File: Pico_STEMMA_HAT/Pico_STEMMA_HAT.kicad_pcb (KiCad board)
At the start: 2 copper layers, 58 x 67 mm, 57 parts, among them J1 Conn_01x20_Socket, J2 Conn_01x20_Socket, J3 SDCARD_MODULE

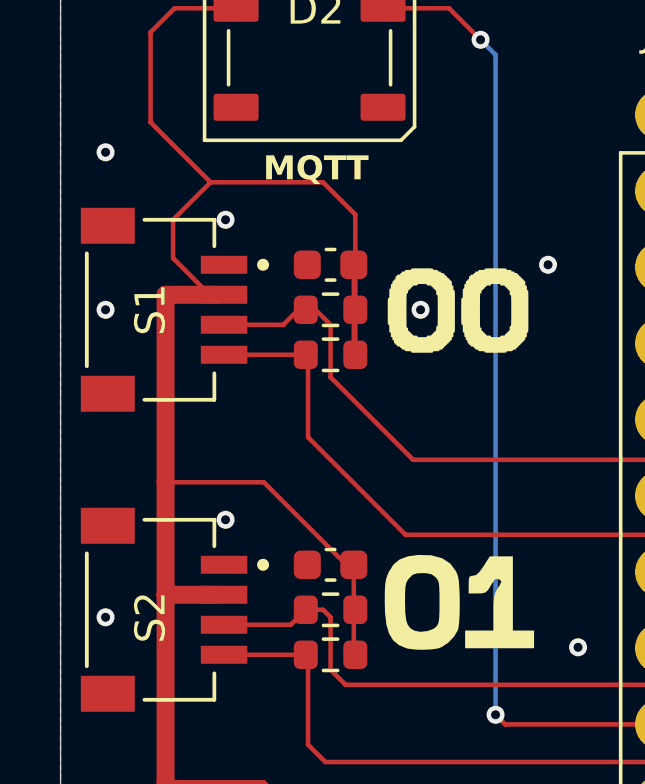
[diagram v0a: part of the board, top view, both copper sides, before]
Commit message: Adjust traces
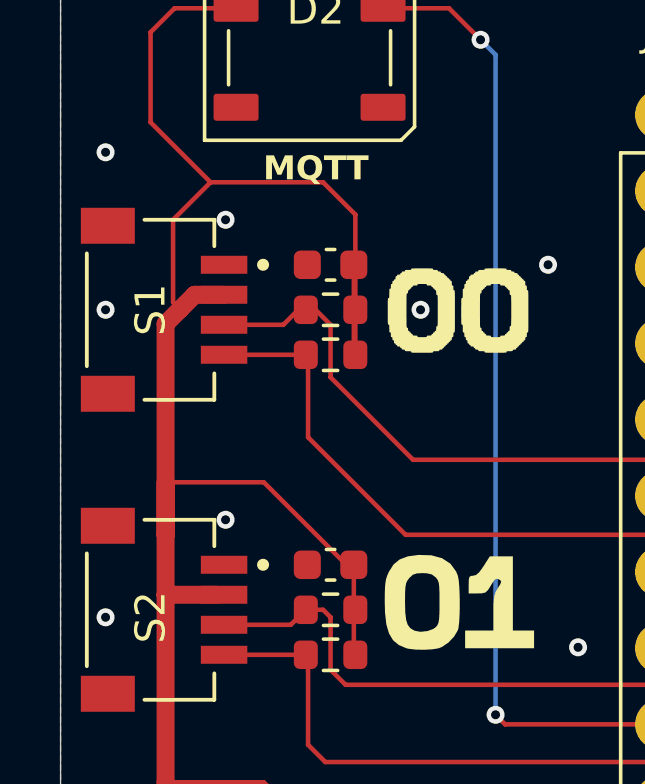
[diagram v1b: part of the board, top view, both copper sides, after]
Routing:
- net +3V3: track 376.0 -> 377.0 mm
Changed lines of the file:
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@@
 		)
 		(property "Value" "0.1 uF"
-			(at 0 1.43 90)
+			(at 1 2 90)
 			(layer "F.Fab")
 			(effects
@@
 		)
 		(property "Value" "4.7k"
-			(at 0 1.43 90)
+			(at -3.25 0 90)
 			(layer "F.Fab")
 			(effects
@@
 		)
 		(property "Value" "4.7k"
-			(at 0 1.43 90)
+			(at -3.25 0 90)
 			(layer "F.Fab")
 			(effects
@@
 	)
 	(segment
+		(start 124.9851 84.9851)
+		(end 125.4702 84.5)
+		(width 0.6)
+		(layer "F.Cu")
+		(net 2)
+	)
+	(segment
+		(start 124.5 94.5)
+		(end 124.5 92.5)
+		(width 0.6)
+		(layer "F.Cu")
+		(net 2)
+	)
+	(segment
 		(start 173 120)
 		(end 169.675 116.675)
@@
 	)
 	(segment
-		(start 126.2 84.5)
-		(end 124.5 84.5)
-		(width 0.6)
-		(layer "F.Cu")
-		(net 2)
-	)
-	(segment
 		(start 130.775 83.5)
 		(end 130.775 86.45)
@@
 	)
 	(segment
+		(start 125.4702 84.5)
+		(end 126.45 84.5)
+		(width 0.6)
+		(layer "F.Cu")
+		(net 2)
+	)
+	(segment
 		(start 148.5 137.5)
 		(end 143 137.5)
@@
 	)
 	(segment
-		(start 124.5 90.75)
-		(end 124.5 84.5)
-		(width 0.6)
-		(layer "F.Cu")
-		(net 2)
-	)
-	(segment
 		(start 169.725 116.5)
 		(end 166.075 116.5)
@@
 	)
 	(segment
+		(start 124.75 84.75)
+		(end 124.9851 84.9851)
+		(width 0.1524)
+		(layer "F.Cu")
+		(net 2)
+	)
+	(segment
 		(start 130.525 93.5)
 		(end 127.775 90.75)
@@
 	)
 	(segment
+		(start 124.5 92.5)
+		(end 124.5 85.4702)
+		(width 0.6)
+		(layer "F.Cu")
+		(net 2)
+	)
+	(segment
 		(start 130.775 103.5)
 		(end 130.775 106.45)
@@
 	)
 	(segment
-		(start 125.971 84.5)
-		(end 124.75 83.279)
-		(width 0.1524)
-		(layer "F.Cu")
-		(net 2)
-	)
-	(segment
 		(start 126 80.75)
 		(end 129.75 80.75)
@@
 	)
 	(segment
-		(start 124.5 94.5)
-		(end 124.5 90.75)
-		(width 0.6)
-		(layer "F.Cu")
-		(net 2)
-	)
-	(segment
-		(start 126.45 84.5)
-		(end 125.971 84.5)
-		(width 0.1524)
-		(layer "F.Cu")
-		(net 2)
-	)
-	(segment
 		(start 174.05 105.5)
 		(end 175.75 105.5)
@@
 	)
 	(segment
-		(start 124.75 82)
-		(end 126 80.75)
-		(width 0.1524)
-		(layer "F.Cu")
-		(net 2)
-	)
-	(segment
 		(start 169.725 83.55)
 		(end 169.725 86.725)
@@
 	)
 	(segment
+		(start 124.5 92.5)
+		(end 124.5 90.75)
+		(width 0.6)
+		(layer "F.Cu")
+		(net 2)
+	)
+	(segment
 		(start 130.525 103.5)
 		(end 127.775 100.75)
@@
 	)
 	(segment
+		(start 124.75 82)
+		(end 124.75 84.75)
+		(width 0.1524)
+		(layer "F.Cu")
+		(net 2)
+	)
+	(segment
 		(start 169.725 86.725)
 		(end 172.5 89.5)
@@
 	)
 	(segment
+		(start 124.5 85.4702)
+		(end 124.9851 84.9851)
+		(width 0.6)
+		(layer "F.Cu")
+		(net 2)
+	)
+	(segment
 		(start 175.75 109.75)
 		(end 173 109.75)
@@
 	)
 	(segment
-		(start 124.75 83.279)
-		(end 124.75 82)
-		(width 0.1524)
-		(layer "F.Cu")
-		(net 2)
-	)
-	(segment
 		(start 157.725 133.5)
 		(end 157.725 136.725)
@@
 		(layer "F.Cu")
 		(net 2)
+	)
+	(segment
+		(start 126 80.75)
+		(end 124.75 82)
+		(width 0.1524)
+		(layer "F.Cu")
+		(net 2)

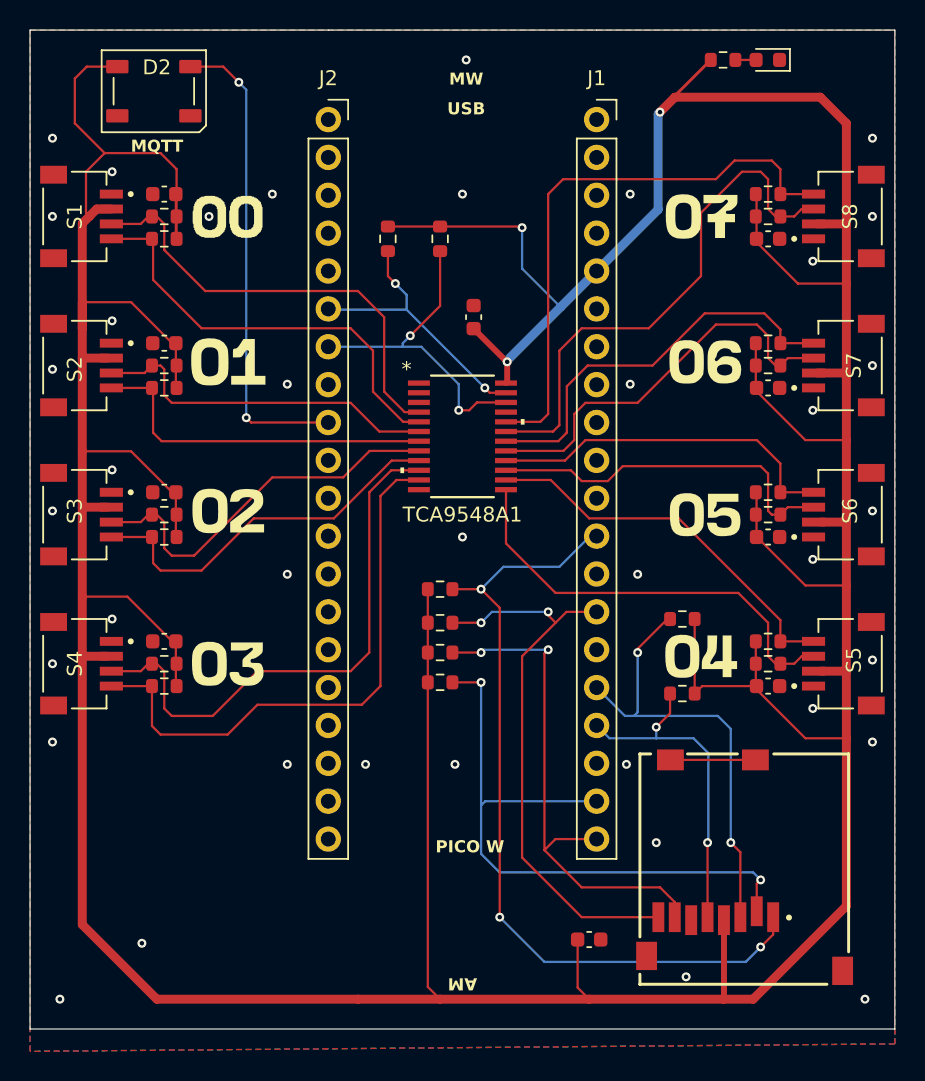
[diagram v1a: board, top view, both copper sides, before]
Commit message: Add the ability to change multiplexer address
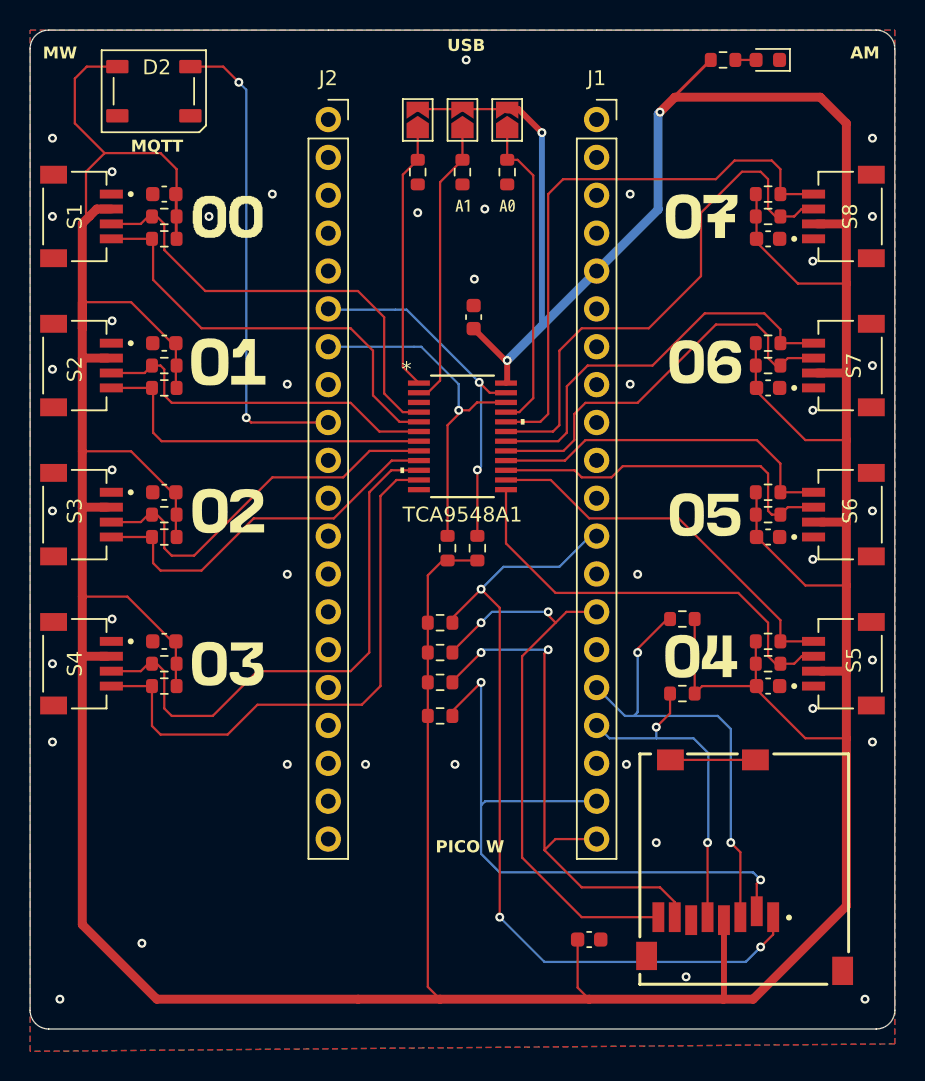
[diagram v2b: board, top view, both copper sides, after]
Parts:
- added JP1: SolderJumper_2_Open, Jumper:SolderJumper-2_P1.3mm_Open_TrianglePad1.0x1.5mm, F.Cu at (153.0, 78.5)
- added JP2: SolderJumper_2_Open, Jumper:SolderJumper-2_P1.3mm_Open_TrianglePad1.0x1.5mm, F.Cu at (150.0, 78.5)
- added JP3: SolderJumper_2_Open, Jumper:SolderJumper-2_P1.3mm_Open_TrianglePad1.0x1.5mm, F.Cu at (147.0, 78.5)
- added R26: 10k, Resistor_SMD:R_0603_1608Metric, F.Cu at (153.0, 82.0)
- added R27: 10k, Resistor_SMD:R_0603_1608Metric, F.Cu at (150.0, 82.0)
- added R28: 10k, Resistor_SMD:R_0603_1608Metric, F.Cu at (147.0, 82.0)
- added kibuzzard-67A6AC81: G***, kibuzzard-67A6AC81, F.Cu at (153.0, 84.3)
- added kibuzzard-67A6AC93: G***, kibuzzard-67A6AC93, F.Cu at (150.0, 84.3)
- moved R25 21.6 mm to (151.0, 107.2), turned to 90 degrees
- moved R24 20.8 mm to (149.0, 107.2), turned to 90 degrees
- moved R20 2.25 mm to (148.5, 118.5)
- moved R21 2.25 mm to (148.5, 112.2)
- moved R22 2.00 mm to (148.5, 114.2)
- moved R23 2.00 mm to (148.5, 116.2)
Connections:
- TCA9548A1 pad 1: unconnected-(TCA9548A1-A0-Pad1) -> /A2
- TCA9548A1 pad 2: unconnected-(TCA9548A1-A1-Pad2) -> /A1
- TCA9548A1 pad 21: unconnected-(TCA9548A1-A2-Pad21) -> /A0
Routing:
- net /A0: track 0.00 -> 21.3 mm
- net /A1: track 0.00 -> 19.1 mm
- net /A2: track 0.00 -> 17.8 mm
- net +3V3: track 377.0 -> 388.6 mm
- net /PICO_SDA: track 18.7 -> 24.7 mm
- net /PICO_SCL: track 22.4 -> 23.7 mm, vias 2 -> 1
- net /GPIO22/DAT2: track 55.2 -> 56.4 mm
- net /GPIO17/CS: track 43.0 -> 44.1 mm
- net /GPIO21/DAT1: track 38.2 -> 39.1 mm
- net /GPIO16/DATA_OUT: track 35.0 -> 35.9 mm
- net GND: vias 39 -> 40
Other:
- outline, holes or cut-outs redrawn

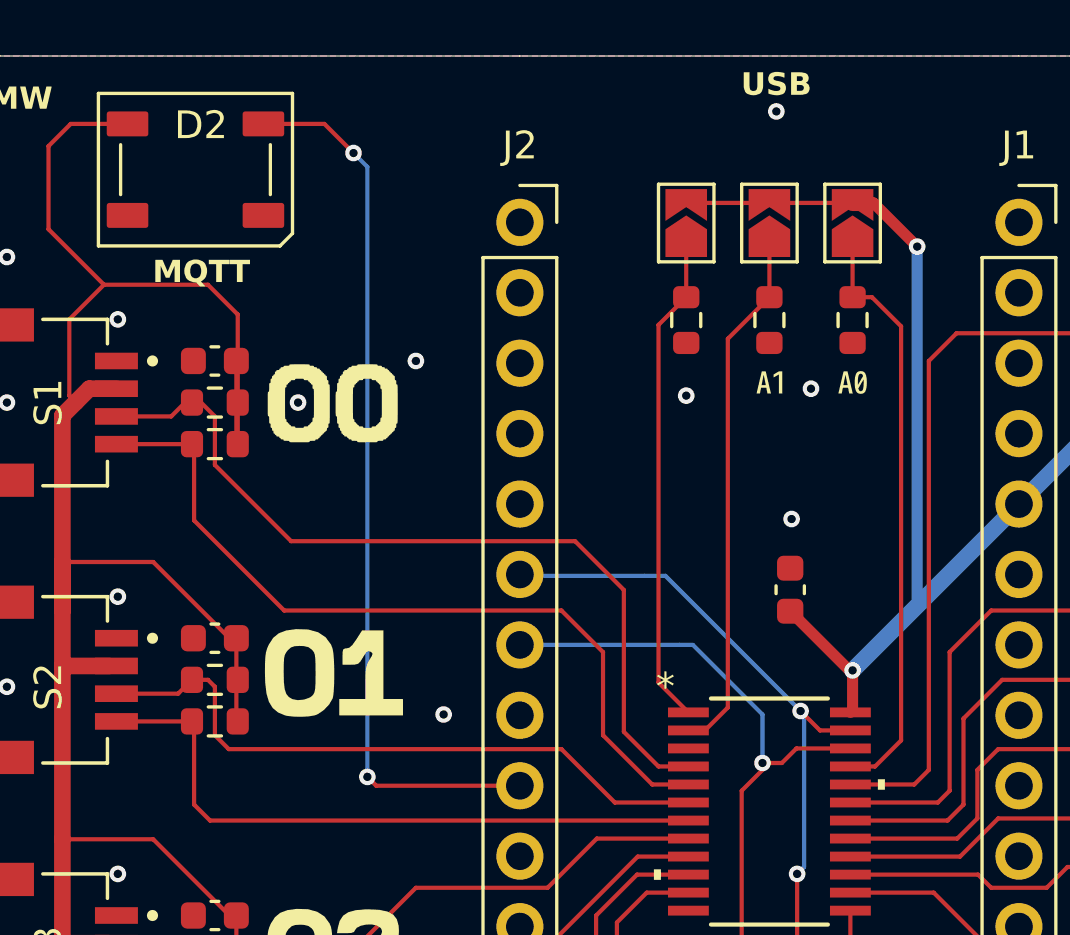
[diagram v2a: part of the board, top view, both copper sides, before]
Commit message: Adjust traces
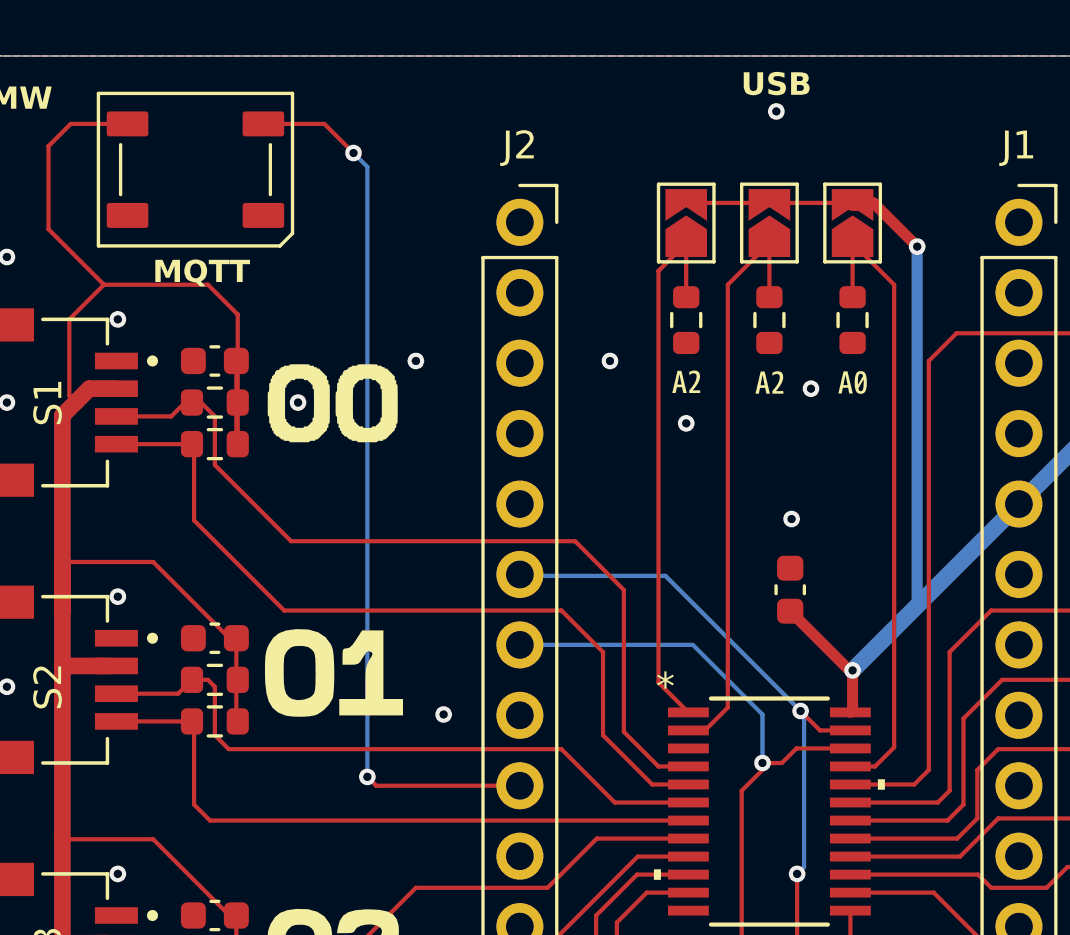
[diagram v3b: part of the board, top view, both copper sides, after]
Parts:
- removed kibuzzard-67A6AC93: G***, kibuzzard-67A6AC93
- added kibuzzard-67A6B8FA: G***, kibuzzard-67A6B8FA, F.Cu at (150.0, 84.3)
- added kibuzzard-67A6B903: G***, kibuzzard-67A6B903, F.Cu at (147.0, 84.2)
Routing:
- net /A2: track 17.8 -> 19.7 mm
- net /A1: track 19.1 -> 21.1 mm
- net /A0: track 21.3 -> 22.6 mm
- net GND: vias 40 -> 41

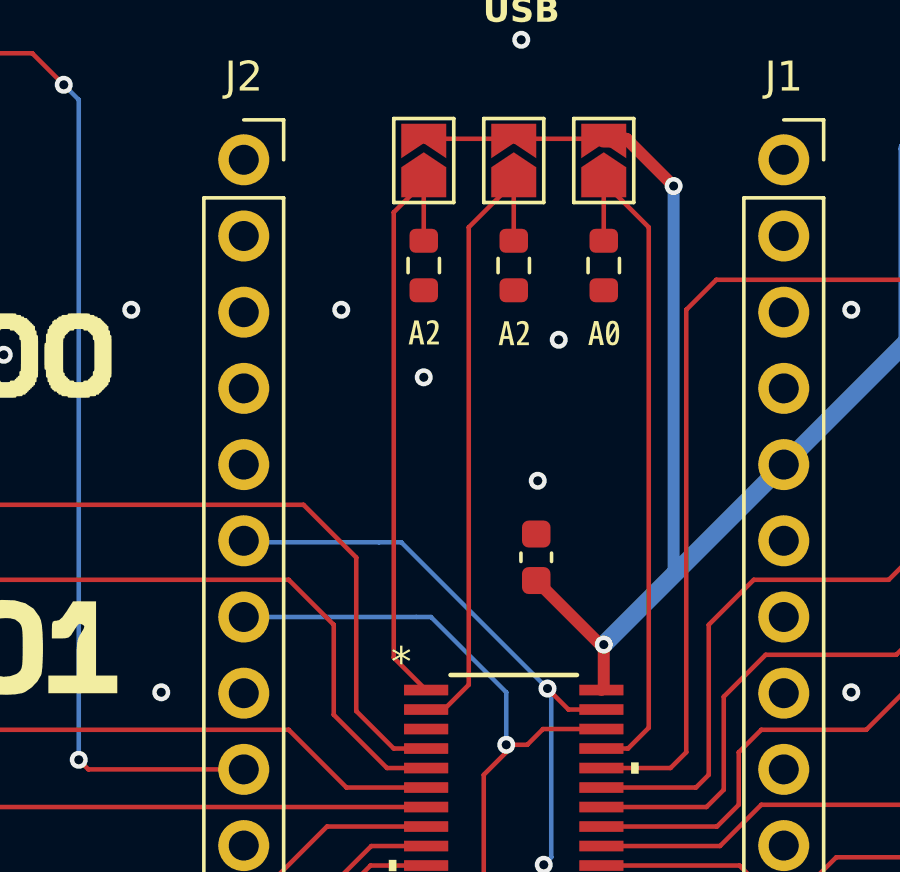
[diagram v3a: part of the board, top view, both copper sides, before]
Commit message: Adjust traces
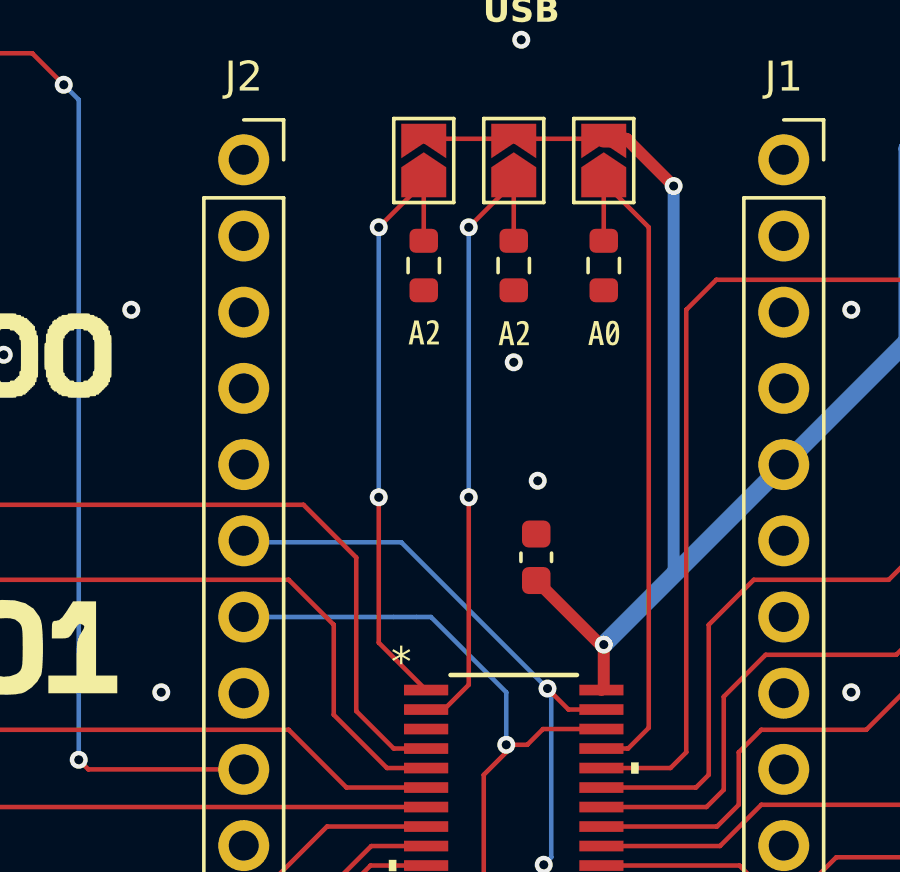
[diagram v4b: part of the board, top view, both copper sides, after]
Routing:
- net /A2: track 19.7 -> 20.2 mm, vias 0 -> 2
- net GND: vias 41 -> 39
- net /A1: vias 0 -> 2
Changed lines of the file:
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@@
 				(font
 					(size 0.001 0.001)
+					(thickness 0.15)
 				)
 			)
@@
 				(font
 					(size 0.001 0.001)
+					(thickness 0.15)
 				)
 			)
@@
 				(font
 					(size 0.001 0.001)
+					(thickness 0.15)
 				)
 			)
@@
 				(font
 					(size 0.001 0.001)
+					(thickness 0.15)
 				)
 			)
@@
 	)
 	(via
-		(at 151.5 84.5)
+		(at 150 85.25)
 		(size 0.6)
 		(drill 0.3)
@@
 	)
 	(via
-		(at 144.25 83.5)
-		(size 0.6)
-		(drill 0.3)
-		(layers "F.Cu" "B.Cu")
-		(free yes)
-		(net 1)
-	)
-	(via
 		(at 173.5 88)
 		(size 0.6)
@@
 	)
 	(via
-		(at 147 85.75)
-		(size 0.6)
-		(drill 0.3)
-		(layers "F.Cu" "B.Cu")
-		(free yes)
-		(net 1)
-	)
-	(via
 		(at 128.5 133.75)
 		(size 0.6)
@@
 	)
 	(segment
-		(start 148.5 80.75)
-		(end 150 79.25)
+		(start 148.5 96)
+		(end 148.5 89.75)
 		(width 0.1524)
 		(layer "F.Cu")
@@
 	)
 	(segment
-		(start 148.5 96)
-		(end 148.5 80.75)
+		(start 148.5 80.75)
+		(end 150 79.25)
 		(width 0.1524)
 		(layer "F.Cu")
 		(net 51)
 	)
+	(via
+		(at 148.5 89.75)
+		(size 0.6)
+		(drill 0.3)
+		(layers "F.Cu" "B.Cu")
+		(net 51)
+	)
+	(via
+		(at 148.5 80.75)
+		(size 0.6)
+		(drill 0.3)
+		(layers "F.Cu" "B.Cu")
+		(net 51)
+	)
+	(segment
+		(start 148.5 89.75)
+		(end 148.5 80.75)
+		(width 0.1524)
+		(layer "B.Cu")
+		(net 51)
+	)
 	(segment
-		(start 146 95.096001)
-		(end 146 80.25)
+		(start 145.5 89.75)
+		(end 145.5 94.596001)
 		(width 0.1524)
 		(layer "F.Cu")
@@
 	)
 	(segment
-		(start 146 80.25)
+		(start 147 81.2)
 		(end 147 79.25)
 		(width 0.1524)
@@
 	)
 	(segment
-		(start 147 81.2)
-		(end 147 79.25)
+		(start 145.5 94.596001)
+		(end 147.079 96.175001)
 		(width 0.1524)
 		(layer "F.Cu")
@@
 	)
 	(segment
-		(start 147.079 96.175001)
-		(end 146 95.096001)
+		(start 145.5 80.75)
+		(end 147 79.25)
 		(width 0.1524)
 		(layer "F.Cu")
 		(net 53)
 	)
+	(via
+		(at 145.5 89.75)
+		(size 0.6)
+		(drill 0.3)
+		(layers "F.Cu" "B.Cu")
+		(net 53)
+	)
+	(via
+		(at 145.5 80.75)
+		(size 0.6)
+		(drill 0.3)
+		(layers "F.Cu" "B.Cu")
+		(net 53)
+	)
+	(segment
+		(start 145.5 89.75)
+		(end 145.5 80.75)
+		(width 0.1524)
+		(layer "B.Cu")
+		(net 53)
+	)
